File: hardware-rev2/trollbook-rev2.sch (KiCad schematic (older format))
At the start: 65 parts, among them CON1 FPGA JTAG, CON2 CPU JTAG, P1 /BR, P2 /CDIS, P3 Audio, P4 ER-CON40HT-1, P5 Power, P6 Peripheral, P7 VGA, P8 Clocks, Q1 2N7002E, Q2 2N7002E, Q3 DMP3030SN-7, U1 MC68040FC33V, U10 ADA4851-4, U11 33 MHz, U12 12.288 MHz, U2 EPF10K50VRC240, U3 EPC2, U4 HY57V561620, U5 HY57V561620, U6 AS7C34098, U7 74LVC138, U8 MCP4902, U9 S25FL204K0TMFI010

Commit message: now only the capacitors left
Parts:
- removed ZD1: 5V1, symbol ZENER
- added Q4, Q5: 2N7002E, Housings_SOT-23_SOT-143_TSOT-6:SOT-23_Handsoldering, symbol Q_NMOS_GSD
- added R30, R31, R32, R33: R, Resistors_SMD:R_0805_HandSoldering, symbol R
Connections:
- wire segments 770 -> 782
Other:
- moved on the sheet: P7
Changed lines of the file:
@@
 L CONN_01X06 P7
 U 1 1 5637931C
-P 11800 3050
-F 0 "P7" H 11800 3400 50  0000 C CNN
-F 1 "VGA" V 11900 3050 50  0000 C CNN
-F 2 "Pin_Headers:Pin_Header_Straight_1x06" H 11800 3050 60  0001 C CNN
-F 3 "" H 11800 3050 60  0000 C CNN
-	1    11800 3050
+P 12400 3050
+F 0 "P7" H 12400 3400 50  0000 C CNN
+F 1 "VGA" V 12500 3050 50  0000 C CNN
+F 2 "Pin_Headers:Pin_Header_Straight_1x06" H 12400 3050 60  0001 C CNN
+F 3 "" H 12400 3050 60  0000 C CNN
+	1    12400 3050
 	1    0    0    -1
 $EndComp
@@
 L GND #PWR047
 U 1 1 5637A31E
-P 11550 3100
-F 0 "#PWR047" H 11550 2850 50  0001 C CNN
-F 1 "GND" H 11550 2950 50  0000 C CNN
-F 2 "" H 11550 3100 60  0000 C CNN
-F 3 "" H 11550 3100 60  0000 C CNN
-	1    11550 3100
+P 12150 3100
+F 0 "#PWR047" H 12150 2850 50  0001 C CNN
+F 1 "GND" H 12150 2950 50  0000 C CNN
+F 2 "" H 12150 3100 60  0000 C CNN
+F 3 "" H 12150 3100 60  0000 C CNN
+	1    12150 3100
 	0    1    1    0
 $EndComp
-Text Label 11050 3300 0    60   ~ 0
+Text Label 11850 4100 1    60   ~ 0
 VGAVSYNC
-Text Label 11050 3200 0    60   ~ 0
+Text Label 11300 4100 1    60   ~ 0
 VGAHSYNC
 Text Label 5900 20750 0    60   ~ 0
@@
 	1    18450 4100
 	0    1    1    0
-$EndComp
-$Comp
-L ZENER ZD1
-U 1 1 563CFEE2
-P 11500 4750
-F 0 "ZD1" H 11500 4850 50  0000 C CNN
-F 1 "5V1" H 11500 4650 50  0000 C CNN
-F 2 "" H 11500 4750 60  0001 C CNN
-F 3 "" H 11500 4750 60  0000 C CNN
-	1    11500 4750
-	0    1    1    0
-$EndComp
-$Comp
-L GND #PWR065
-U 1 1 563D00D7
-P 11500 5000
-F 0 "#PWR065" H 11500 4750 50  0001 C CNN
-F 1 "GND" H 11500 4850 50  0000 C CNN
-F 2 "" H 11500 5000 60  0000 C CNN
-F 3 "" H 11500 5000 60  0000 C CNN
-	1    11500 5000
-	1    0    0    -1
 $EndComp
 Wire Wire Line
@@
 Connection ~ 8000 2050
 Wire Wire Line
-	11600 2800 11300 2800
+	11300 2800 12200 2800
 Wire Wire Line
 	11300 2800 11300 1350
@@
 	11100 2650 11100 2900
 Wire Wire Line
-	11100 2900 11600 2900
+	11100 2900 12200 2900
 Wire Wire Line
 	10850 4000 10850 3000
 Wire Wire Line
-	10850 3000 11600 3000
-Wire Wire Line
-	11600 3200 11050 3200
-Wire Wire Line
-	11600 3300 11050 3300
-Wire Wire Line
-	11600 3100 11550 3100
+	10850 3000 12200 3000
 Wire Wire Line
 	5700 20750 6500 20750
@@
 Wire Wire Line
 	18650 4100 18450 4100
-Wire Wire Line
-	11500 4950 11500 5000
 Wire Wire Line
 	11700 16100 12400 16100
@@
 Connection ~ 4050 17550
 $Comp
-L +3V3 #PWR066
+L +3V3 #PWR065
 U 1 1 563DA482
 P 4050 17400
-F 0 "#PWR066" H 4050 17250 50  0001 C CNN
+F 0 "#PWR065" H 4050 17250 50  0001 C CNN
 F 1 "+3V3" H 4050 17540 50  0000 C CNN
 F 2 "" H 4050 17400 60  0000 C CNN
@@
 Connection ~ 25600 15050
 $Comp
-L +3V3 #PWR067
+L +3V3 #PWR066
 U 1 1 563F88B3
 P 25550 14900
-F 0 "#PWR067" H 25550 14750 50  0001 C CNN
+F 0 "#PWR066" H 25550 14750 50  0001 C CNN
 F 1 "+3V3" H 25550 15040 50  0000 C CNN
 F 2 "" H 25550 14900 60  0000 C CNN
@@
 Connection ~ 18650 5100
 $Comp
-L GND #PWR068
+L GND #PWR067
 U 1 1 5640F001
 P 13950 3250
-F 0 "#PWR068" H 13950 3000 50  0001 C CNN
+F 0 "#PWR067" H 13950 3000 50  0001 C CNN
 F 1 "GND" H 13950 3100 50  0000 C CNN
 F 2 "" H 13950 3250 60  0000 C CNN
@@
 $EndComp
 $Comp
-L +3V3 #PWR069
+L +3V3 #PWR068
 U 1 1 56412F98
 P 25250 14200
-F 0 "#PWR069" H 25250 14050 50  0001 C CNN
+F 0 "#PWR068" H 25250 14050 50  0001 C CNN
 F 1 "+3V3" H 25250 14340 50  0000 C CNN
 F 2 "" H 25250 14200 60  0000 C CNN
@@
 	25200 14200 25250 14200
 $Comp
-L GND #PWR070
+L GND #PWR069
 U 1 1 56417AE4
 P 27300 16150
-F 0 "#PWR070" H 27300 15900 50  0001 C CNN
+F 0 "#PWR069" H 27300 15900 50  0001 C CNN
 F 1 "GND" H 27300 16000 50  0000 C CNN
 F 2 "" H 27300 16150 60  0000 C CNN
@@
 NoConn ~ 26750 15850
 $Comp
-L GND #PWR071
+L GND #PWR070
 U 1 1 5641955C
 P 5700 18650
-F 0 "#PWR071" H 5700 18400 50  0001 C CNN
+F 0 "#PWR070" H 5700 18400 50  0001 C CNN
 F 1 "GND" H 5700 18500 50  0000 C CNN
 F 2 "" H 5700 18650 60  0000 C CNN
@@
 	2900 21050 3600 21050
 $Comp
-L +3V3 #PWR072
+L +3V3 #PWR071
 U 1 1 5655A0BD
 P 12000 18750
-F 0 "#PWR072" H 12000 18600 50  0001 C CNN
+F 0 "#PWR071" H 12000 18600 50  0001 C CNN
 F 1 "+3V3" H 12000 18890 50  0000 C CNN
 F 2 "" H 12000 18750 60  0000 C CNN
@@
 	12000 19000 12100 19000
 $Comp
-L +3V3 #PWR073
+L +3V3 #PWR072
 U 1 1 5655CFA8
 P 14850 18850
-F 0 "#PWR073" H 14850 18700 50  0001 C CNN
+F 0 "#PWR072" H 14850 18700 50  0001 C CNN
 F 1 "+3V3" H 14850 18990 50  0000 C CNN
 F 2 "" H 14850 18850 60  0000 C CNN
@@
 Wire Wire Line
 	14850 18850 14850 19100
+$Comp
+L Q_NMOS_GSD Q4
+U 1 1 569D1361
+P 11500 3600
+F 0 "Q4" H 11400 3650 50  0000 R CNN
+F 1 "2N7002E" H 11550 3750 50  0000 R CNN
+F 2 "Housings_SOT-23_SOT-143_TSOT-6:SOT-23_Handsoldering" H 11700 3700 29  0001 C CNN
+F 3 "" H 11500 3600 60  0000 C CNN
+	1    11500 3600
+	1    0    0    -1
+$EndComp
+$Comp
+L Q_NMOS_GSD Q5
+U 1 1 569D34CC
+P 12050 3600
+F 0 "Q5" H 11950 3650 50  0000 R CNN
+F 1 "2N7002E" H 12100 3750 50  0000 R CNN
+F 2 "Housings_SOT-23_SOT-143_TSOT-6:SOT-23_Handsoldering" H 12250 3700 29  0001 C CNN
+F 3 "" H 12050 3600 60  0000 C CNN
+	1    12050 3600
+	1    0    0    -1
+$EndComp
+Wire Wire Line
+	12200 3100 12150 3100
+Wire Wire Line
+	12100 3300 12200 3300
+Wire Wire Line
+	12150 3300 12150 3400
+Wire Wire Line
+	11550 3200 12200 3200
+Wire Wire Line
+	11600 3200 11600 3400
+$Comp
+L GND #PWR073
+U 1 1 569D5BFA
+P 12150 3850
+F 0 "#PWR073" H 12150 3600 50  0001 C CNN
+F 1 "GND" H 12150 3700 50  0000 C CNN
+F 2 "" H 12150 3850 60  0000 C CNN
+F 3 "" H 12150 3850 60  0000 C CNN
+	1    12150 3850
+	1    0    0    -1
+$EndComp
+$Comp
+L GND #PWR074
+U 1 1 569D5CD8
+P 11600 3850
+F 0 "#PWR074" H 11600 3600 50  0001 C CNN
+F 1 "GND" H 11600 3700 50  0000 C CNN
+F 2 "" H 11600 3850 60  0000 C CNN
+F 3 "" H 11600 3850 60  0000 C CNN
+	1    11600 3850
+	1    0    0    -1
+$EndComp
+$Comp
+L +3V3 #PWR075
+U 1 1 569D5D6D
+P 11750 3300
+F 0 "#PWR075" H 11750 3150 50  0001 C CNN
+F 1 "+3V3" H 11750 3440 50  0000 C CNN
+F 2 "" H 11750 3300 60  0000 C CNN
+F 3 "" H 11750 3300 60  0000 C CNN
+	1    11750 3300
+	0    -1   -1   0
+$EndComp
+$Comp
+L R R33
+U 1 1 569D5F5D
+P 11950 3300
+F 0 "R33" V 12030 3300 50  0000 C CNN
+F 1 "R" V 11950 3300 50  0000 C CNN
+F 2 "Resistors_SMD:R_0805_HandSoldering" V 11880 3300 30  0001 C CNN
+F 3 "" H 11950 3300 30  0000 C CNN
+	1    11950 3300
+	0    1    1    0
+$EndComp
+Connection ~ 12150 3300
+Wire Wire Line
+	11800 3300 11750 3300
+$Comp
+L R R31
+U 1 1 569D6A3F
+P 11400 3200
+F 0 "R31" V 11480 3200 50  0000 C CNN
+F 1 "R" V 11400 3200 50  0000 C CNN
+F 2 "Resistors_SMD:R_0805_HandSoldering" V 11330 3200 30  0001 C CNN
+F 3 "" H 11400 3200 30  0000 C CNN
+	1    11400 3200
+	0    1    1    0
+$EndComp
+Connection ~ 11600 3200
+$Comp
+L +3V3 #PWR076
+U 1 1 569D6F30
+P 11200 3200
+F 0 "#PWR076" H 11200 3050 50  0001 C CNN
+F 1 "+3V3" H 11200 3340 50  0000 C CNN
+F 2 "" H 11200 3200 60  0000 C CNN
+F 3 "" H 11200 3200 60  0000 C CNN
+	1    11200 3200
+	0    -1   -1   0
+$EndComp
+Wire Wire Line
+	11250 3200 11200 3200
+$Comp
+L R R30
+U 1 1 569D740E
+P 11200 3400
+F 0 "R30" V 11280 3400 50  0000 C CNN
+F 1 "R" V 11200 3400 50  0000 C CNN
+F 2 "Resistors_SMD:R_0805_HandSoldering" V 11130 3400 30  0001 C CNN
+F 3 "" H 11200 3400 30  0000 C CNN
+	1    11200 3400
+	-1   0    0    1
+$EndComp
+$Comp
+L R R32
+U 1 1 569D7535
+P 11750 3500
+F 0 "R32" V 11830 3500 50  0000 C CNN
+F 1 "R" V 11750 3500 50  0000 C CNN
+F 2 "Resistors_SMD:R_0805_HandSoldering" V 11680 3500 30  0001 C CNN
+F 3 "" H 11750 3500 30  0000 C CNN
+	1    11750 3500
+	-1   0    0    1
+$EndComp
+Wire Wire Line
+	11750 3650 11850 3650
+Wire Wire Line
+	11850 3600 11850 4100
+Wire Wire Line
+	11750 3300 11750 3350
+Wire Wire Line
+	11200 3200 11200 3250
+Wire Wire Line
+	11300 3600 11200 3600
+Wire Wire Line
+	11200 3600 11200 3550
+Connection ~ 11850 3650
+Wire Wire Line
+	11300 3600 11300 4100
+Wire Wire Line
+	12150 3800 12150 3850
+Wire Wire Line
+	11600 3800 11600 3850
 $EndSCHEMATC

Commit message: capacitors, capacitors everywhere
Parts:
- added C1: 220u, Capacitors_SMD:c_elec_6.3x7.7, symbol CP
- added C10, C11, C12, C13, C14, C15, C16, C17, C18, C19, C20, C21, C22, C23, C24, C25, C26, C27, C28, C29, C3, C30, C31, C32, C33, C34, C35, C36, C4, C5, C6, C67, C68, C69, C7, C70, C71, C8, C9: 100n, Capacitors_SMD:C_0805_HandSoldering, symbol C
- added C2: 10u, Capacitors_SMD:C_1206_HandSoldering, symbol C
- added C37, C38, C39, C40, C41, C42, C43, C44, C45, C46, C47, C48, C49, C50, C51, C52, C53, C54, C55, C56, C57, C58, C59, C60, C61, C62, C63, C64, C65, C66: 10n, Capacitors_SMD:C_0805_HandSoldering, symbol C
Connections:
- wire segments 782 -> 891

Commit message: added external interrupt header
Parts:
- added P9: CONN_01X05, Pin_Headers:Pin_Header_Straight_1x05, symbol CONN_01X05
- added RP11: R_PACK4, mod:RPACK8_SMD, symbol R_PACK4
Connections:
- net labels added: AUDIOL, AUDIOR
- wire segments 891 -> 899
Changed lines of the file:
@@
 	1    0    0    -1
 $EndComp
-Text Label 3000 20750 0    60   ~ 0
+Text Label 3000 21050 0    60   ~ 0
 EXTINT0
-Text Label 3000 20850 0    60   ~ 0
-EXTINT1
 Text Label 3000 20950 0    60   ~ 0
+EXTINT1
+Text Label 3000 20850 0    60   ~ 0
 EXTINT2
-Text Label 3000 21050 0    60   ~ 0
+Text Label 3000 20750 0    60   ~ 0
 EXTINT3
 $Comp
@@
 Connection ~ 5700 18450
 Wire Wire Line
-	2900 20750 3600 20750
+	2900 20750 3650 20750
 Wire Wire Line
-	2900 20850 3600 20850
+	2900 20850 3750 20850
 Wire Wire Line
-	2900 20950 3600 20950
+	2900 20950 3850 20950
 Wire Wire Line
-	2900 21050 3600 21050
+	2900 21050 3950 21050
 Wire Wire Line
 	12000 18750 12000 19000
@@
 	28700 7100 28700 7050
 Connection ~ 28300 7100
+$Comp
+L CONN_01X05 P9
+U 1 1 56B0EAA5
+P 2700 20950
+F 0 "P9" H 2619 20518 50  0000 C CNN
+F 1 "CONN_01X05" H 2619 20610 50  0000 C CNN
+F 2 "Pin_Headers:Pin_Header_Straight_1x05" H 2700 20950 50  0001 C CNN
+F 3 "" H 2700 20950 50  0000 C CNN
+	1    2700 20950
+	-1   0    0    1
+$EndComp
+$Comp
+L GND #PWR0109
+U 1 1 56B0EE15
+P 2950 21200
+F 0 "#PWR0109" H 2950 20950 50  0001 C CNN
+F 1 "GND" H 2958 21026 50  0000 C CNN
+F 2 "" H 2950 21200 50  0000 C CNN
+F 3 "" H 2950 21200 50  0000 C CNN
+	1    2950 21200
+	1    0    0    -1
+$EndComp
+Wire Wire Line
+	2950 21200 2950 21150
+Wire Wire Line
+	2950 21150 2900 21150
+$Comp
+L R_PACK4 RP11
+U 1 1 56B0F57C
+P 3600 20500
+F 0 "RP11" V 3554 20928 50  0000 L CNN
+F 1 "R_PACK4" V 3646 20928 50  0000 L CNN
+F 2 "mod:RPACK8_SMD" H 3600 20500 50  0001 C CNN
+F 3 "" H 3600 20500 50  0000 C CNN
+	1    3600 20500
+	0    1    1    0
+$EndComp
+$Comp
+L +3V3 #PWR0110
+U 1 1 56B0F7BA
+P 3800 20200
+F 0 "#PWR0110" H 3800 20050 50  0001 C CNN
+F 1 "+3V3" H 3818 20374 50  0000 C CNN
+F 2 "" H 3800 20200 50  0000 C CNN
+F 3 "" H 3800 20200 50  0000 C CNN
+	1    3800 20200
+	1    0    0    -1
+$EndComp
+Wire Wire Line
+	3650 20300 3950 20300
+Connection ~ 3750 20300
+Connection ~ 3850 20300
+Wire Wire Line
+	3800 20300 3800 20200
+Connection ~ 3800 20300
+Wire Wire Line
+	3650 20750 3650 20700
+Wire Wire Line
+	3750 20850 3750 20700
+Wire Wire Line
+	3850 20950 3850 20700
+Wire Wire Line
+	3950 21050 3950 20700
+Text Label 9650 25100 0    60   ~ 0
+AUDIOL
+Text Label 9650 25400 0    60   ~ 0
+AUDIOR
 $EndSCHEMATC

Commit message: finished all routing, only minor touch-ups left
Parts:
- added R34, R35, R36: 10k, Resistors_SMD:R_0805_HandSoldering, symbol R
- added unit 4 of U10
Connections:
- wire segments 899 -> 906
- no-connect marks 27 -> 29
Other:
- note added: "connect 3v3 to vgadisp"
- note removed: "5V sync?"
- note removed: "all these can be user io"
- note removed: "might need backlight pwm here"
- note removed: "might need some pullups here somewhere"
- note removed: "pull down clken"
- note removed: "pull up chip enable"
- note removed: "todo: check pinout"

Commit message: touched up silkscreen a bit
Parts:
- P9: value CONN_01X05 -> Ext. Interrupt
- RP10, RP11, RP9: value R_PACK4 -> 10k
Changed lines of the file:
@@
 P 3850 17750
 F 0 "RP9" H 3850 18200 50  0000 C CNN
-F 1 "R_PACK4" H 3850 17700 50  0000 C CNN
+F 1 "10k" H 3850 17700 50  0000 C CNN
 F 2 "mod:RPACK8_SMD" H 3850 17750 60  0001 C CNN
 F 3 "" H 3850 17750 60  0000 C CNN
@@
 P 25350 15250
 F 0 "RP10" H 25350 15700 50  0000 C CNN
-F 1 "R_PACK4" H 25350 15200 50  0000 C CNN
+F 1 "10k" H 25350 15200 50  0000 C CNN
 F 2 "mod:RPACK8_SMD" H 25350 15250 60  0001 C CNN
 F 3 "" H 25350 15250 60  0000 C CNN
@@
 P 2700 20950
 F 0 "P9" H 2619 20518 50  0000 C CNN
-F 1 "CONN_01X05" H 2619 20610 50  0000 C CNN
+F 1 "Ext. Interrupt" H 2619 20610 50  0000 C CNN
 F 2 "Pin_Headers:Pin_Header_Straight_1x05" H 2700 20950 50  0001 C CNN
 F 3 "" H 2700 20950 50  0000 C CNN
@@
 P 3600 20500
 F 0 "RP11" V 3554 20928 50  0000 L CNN
-F 1 "R_PACK4" V 3646 20928 50  0000 L CNN
+F 1 "10k" V 3646 20928 50  0000 L CNN
 F 2 "mod:RPACK8_SMD" H 3600 20500 50  0001 C CNN
 F 3 "" H 3600 20500 50  0000 C CNN

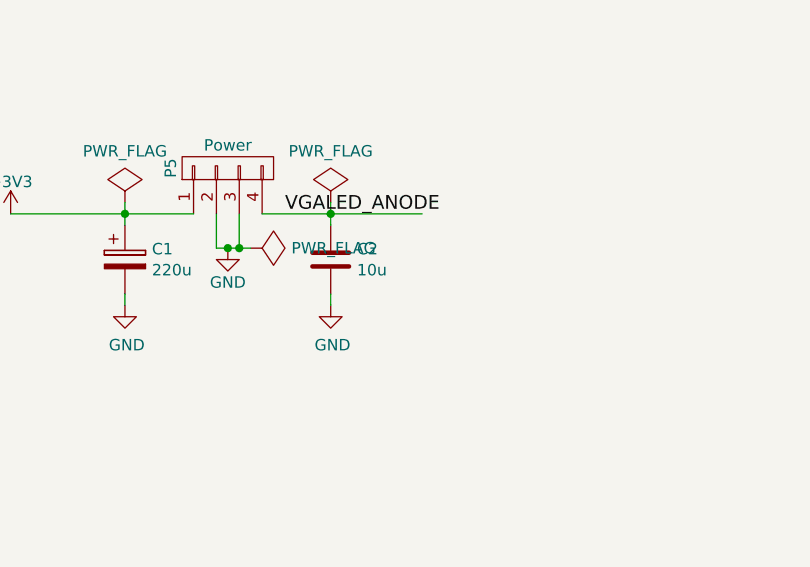
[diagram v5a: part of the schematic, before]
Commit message: added pcb logo
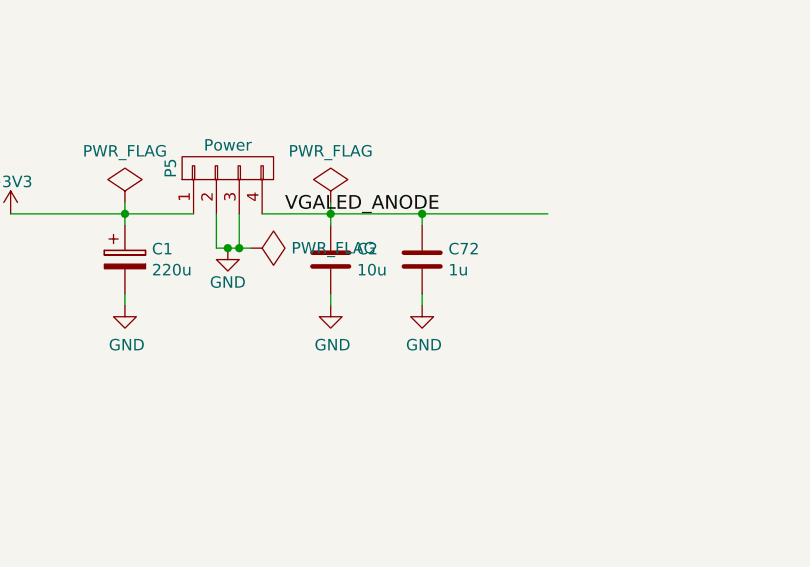
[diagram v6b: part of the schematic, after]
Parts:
- added C72: 1u, Capacitors_SMD:C_1206_HandSoldering, symbol C
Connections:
- wire segments 906 -> 908
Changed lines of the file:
@@
 	2500 22600 1700 22600
 Wire Wire Line
-	2800 22600 3500 22600
+	2800 22600 4050 22600
 Wire Wire Line
 	6500 20250 5600 20250
@@
 $EndComp
 Connection ~ 2700 22750
+$Comp
+L C C72
+U 1 1 56D032F9
+P 3500 22800
+F 0 "C72" H 3615 22846 50  0000 L CNN
+F 1 "1u" H 3615 22754 50  0000 L CNN
+F 2 "Capacitors_SMD:C_1206_HandSoldering" H 3538 22650 50  0001 C CNN
+F 3 "" H 3500 22800 50  0000 C CNN
+	1    3500 22800
+	1    0    0    -1
+$EndComp
+Wire Wire Line
+	3500 22650 3500 22600
+Connection ~ 3500 22600
+$Comp
+L GND #PWR0118
+U 1 1 56D03EB3
+P 3500 23000
+F 0 "#PWR0118" H 3500 22750 50  0001 C CNN
+F 1 "GND" H 3508 22826 50  0000 C CNN
+F 2 "" H 3500 23000 50  0000 C CNN
+F 3 "" H 3500 23000 50  0000 C CNN
+	1    3500 23000
+	1    0    0    -1
+$EndComp
+Wire Wire Line
+	3500 23000 3500 22950
 $EndSCHEMATC

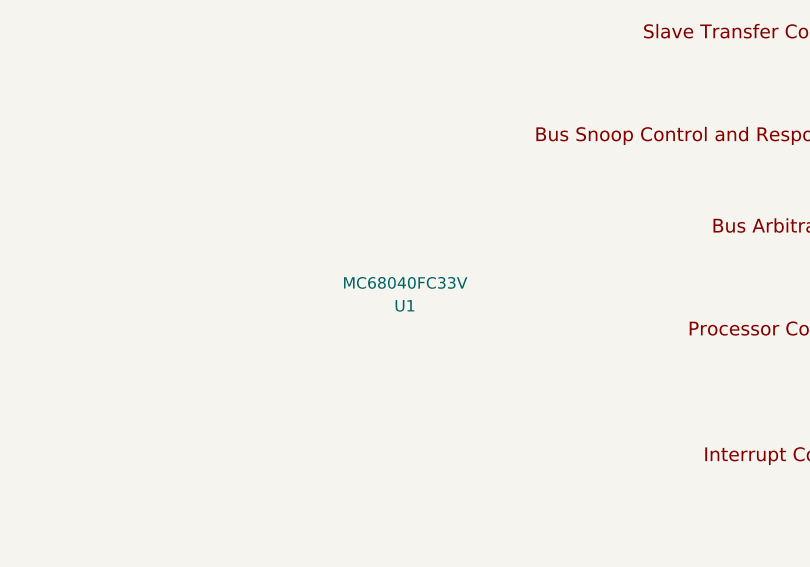
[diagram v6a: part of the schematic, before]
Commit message: correct cpu name on silk screen
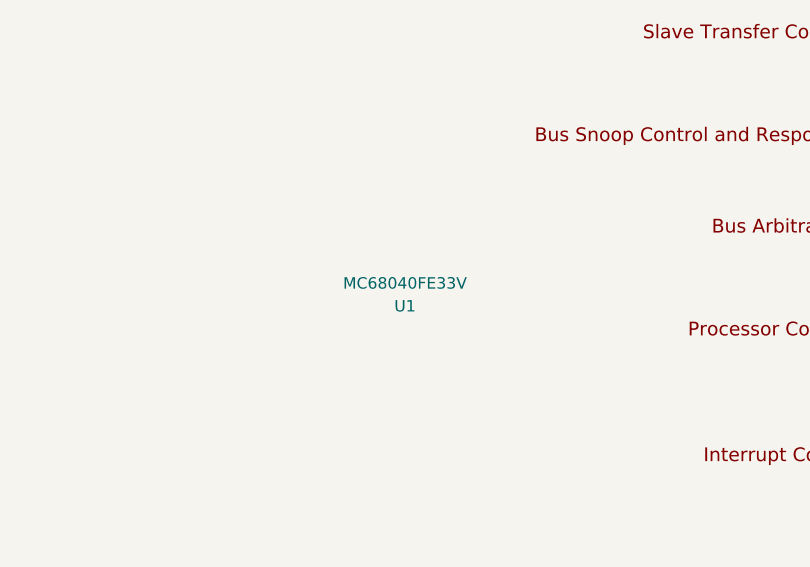
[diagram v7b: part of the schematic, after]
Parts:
- U1: value MC68040FC33V -> MC68040FE33V
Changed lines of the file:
@@
 P 21550 11800
 F 0 "U1" H 21550 11750 50  0000 C CNN
-F 1 "MC68040FC33V" H 21550 11850 50  0000 C CNN
+F 1 "MC68040FE33V" H 21550 11850 50  0000 C CNN
 F 2 "mod:QFP-184" H 21550 11400 50  0001 C CNN
 F 3 "DOCUMENTATION" H 21550 11300 50  0001 C CNN
